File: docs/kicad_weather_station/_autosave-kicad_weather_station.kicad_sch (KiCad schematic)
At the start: 3 parts, among them U1 DHT11

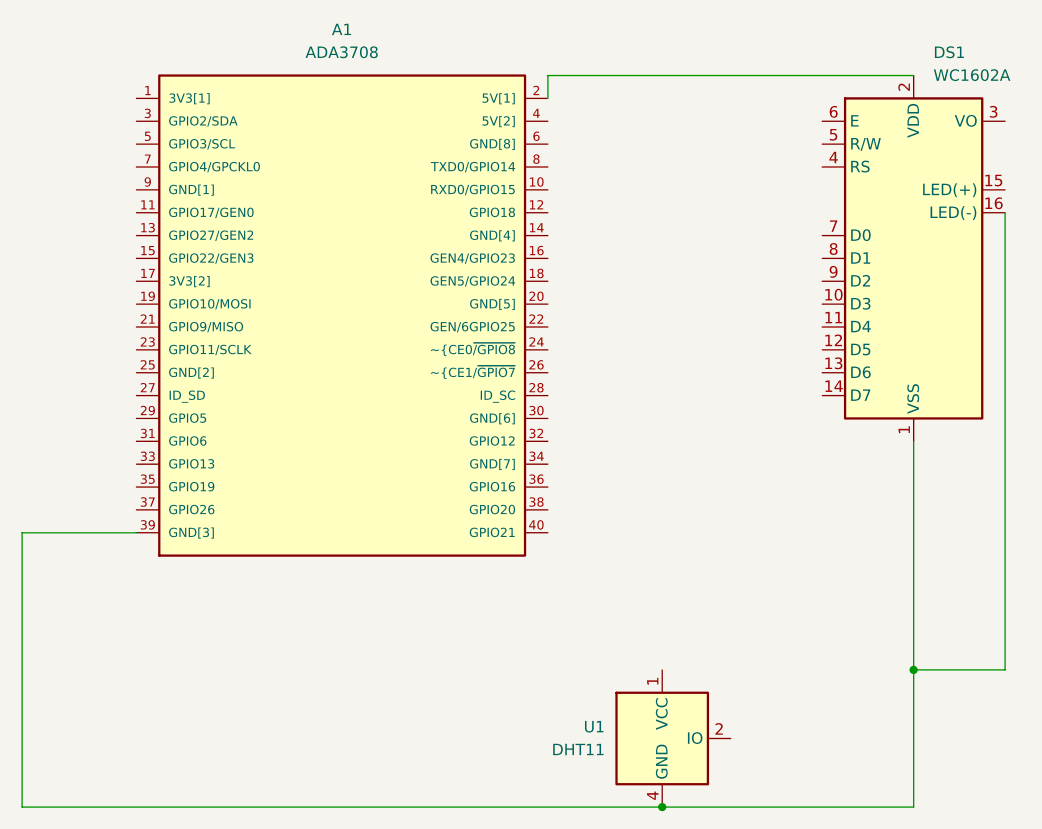
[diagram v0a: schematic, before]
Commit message: Updated README.md and updated parseString code
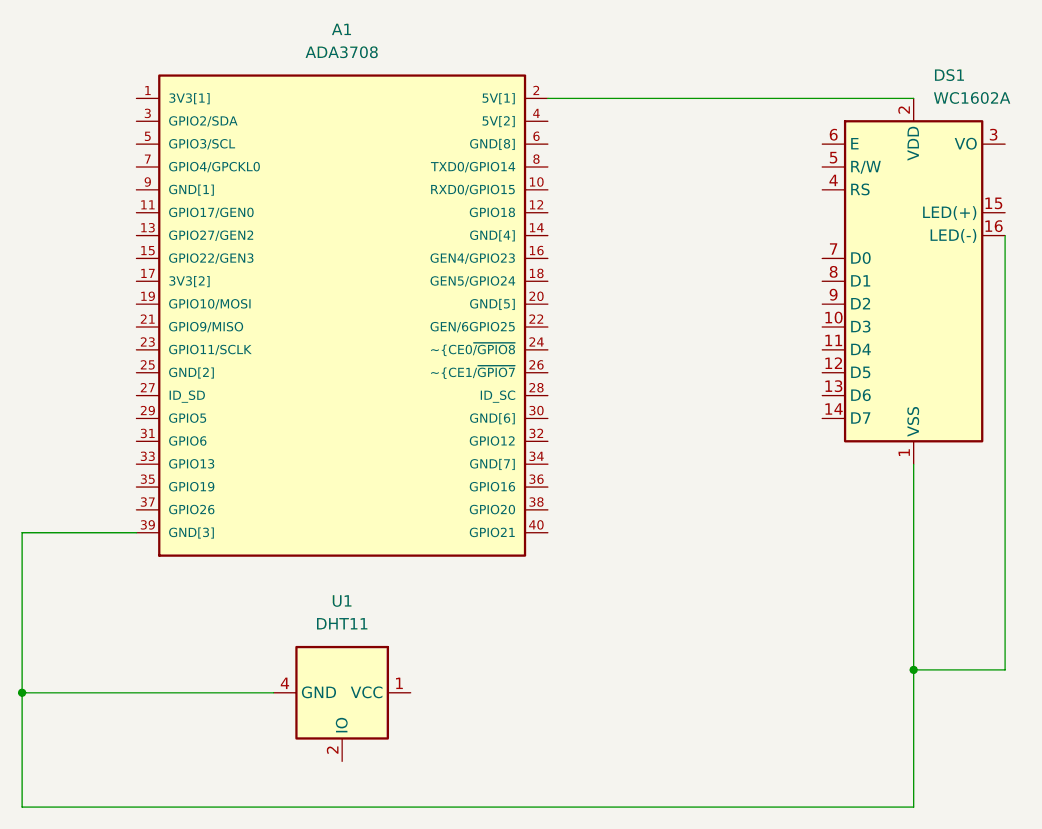
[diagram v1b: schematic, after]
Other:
- moved on the sheet: DS1, U1
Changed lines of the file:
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@@
 (kicad_sch (version 20230121) (generator eeschema)
   (paper "A4")
+  (junction (at 33.02 104.14) (diameter 0) (color 0 0 0 0)
+  )
   (junction (at 132.08 101.6) (diameter 0) (color 0 0 0 0)
   )
-  (junction (at 104.14 116.84) (diameter 0) (color 0 0 0 0)
-  )
-  (wire (pts (xy 104.14 116.84) (xy 33.02 116.84))
+  (wire (pts (xy 132.08 38.1) (xy 91.44 38.1))
     (stroke (width 0) (type default))
   )
-  (wire (pts (xy 132.08 35.56) (xy 91.44 35.56))
-    (stroke (width 0) (type default))
-  )
-  (wire (pts (xy 132.08 116.84) (xy 132.08 101.6))
-    (stroke (width 0) (type default))
-  )
-  (wire (pts (xy 33.02 116.84) (xy 33.02 86.36))
-    (stroke (width 0) (type default))
-  )
-  (wire (pts (xy 104.14 116.84) (xy 132.08 116.84))
+  (wire (pts (xy 33.02 86.36) (xy 33.02 104.14))
     (stroke (width 0) (type default))
   )
@@
     (stroke (width 0) (type default))
   )
-  (wire (pts (xy 142.24 50.8) (xy 142.24 101.6))
+  (wire (pts (xy 33.02 104.14) (xy 60.96 104.14))
+    (stroke (width 0) (type default))
+  )
+  (wire (pts (xy 142.24 53.34) (xy 142.24 101.6))
     (stroke (width 0) (type default))
   )
@@
     (stroke (width 0) (type default))
   )
-  (wire (pts (xy 91.44 35.56) (xy 91.44 38.1))
+  (wire (pts (xy 33.02 116.84) (xy 33.02 104.14))
     (stroke (width 0) (type default))
   )
-  (wire (pts (xy 132.08 76.2) (xy 132.08 101.6))
+  (wire (pts (xy 132.08 101.6) (xy 132.08 116.84))
     (stroke (width 0) (type default))
   )
-  (symbol (lib_id "Display_Character:WC1602A") (at 132.08 55.88 0) (unit 1)
+  (wire (pts (xy 132.08 78.74) (xy 132.08 101.6))
+    (stroke (width 0) (type default))
+  )
+  (wire (pts (xy 132.08 116.84) (xy 33.02 116.84))
+    (stroke (width 0) (type default))
+  )
+  (symbol (lib_id "Display_Character:WC1602A") (at 132.08 58.42 0) (unit 1)
     (in_bom yes) (on_board yes) (dnp no) (fields_autoplaced)
-    (property "Reference" "DS1" (at 134.2741 33.02 0)
+    (property "Reference" "DS1" (at 134.2741 35.56 0)
       (effects (font (size 1.27 1.27)) (justify left))
     )
-    (property "Value" "WC1602A" (at 134.2741 35.56 0)
+    (property "Value" "WC1602A" (at 134.2741 38.1 0)
       (effects (font (size 1.27 1.27)) (justify left))
     )
-    (property "Footprint" "TextBasedDisplay:WC1602A" (at 132.08 78.74 0)
+    (property "Footprint" "TextBasedDisplay:WC1602A" (at 132.08 81.28 0)
       (effects (font (size 1.27 1.27) italic) hide)
     )
-    (property "Datasheet" "http://www.wincomlcd.com/pdf/WC1602A-SFYLYHTC06.pdf" (at 149.86 55.88 0)
+    (property "Datasheet" "http://www.wincomlcd.com/pdf/WC1602A-SFYLYHTC06.pdf" (at 149.86 58.42 0)
       (effects (font (size 1.27 1.27)) hide)
     )
@@
     )
   )
-  (symbol (lib_id "Sensor:DHT11") (at 104.14 109.22 0) (unit 1)
+  (symbol (lib_id "Sensor:DHT11") (at 68.58 104.14 270) (unit 1)
     (in_bom yes) (on_board yes) (dnp no) (fields_autoplaced)
-    (property "Reference" "U1" (at 97.79 107.95 0)
-      (effects (font (size 1.27 1.27)) (justify right))
+    (property "Reference" "U1" (at 68.58 93.98 90)
+      (effects (font (size 1.27 1.27)))
     )
-    (property "Value" "DHT11" (at 97.79 110.49 0)
-      (effects (font (size 1.27 1.27)) (justify right))
+    (property "Value" "DHT11" (at 68.58 96.52 90)
+      (effects (font (size 1.27 1.27)))
     )
-    (property "Footprint" "Sensor:Aosong_DHT11_5.5x12.0_P2.54mm" (at 104.14 119.38 0)
+    (property "Footprint" "Sensor:Aosong_DHT11_5.5x12.0_P2.54mm" (at 58.42 104.14 0)
       (effects (font (size 1.27 1.27)) hide)
     )
-    (property "Datasheet" "http://akizukidenshi.com/download/ds/aosong/DHT11.pdf" (at 107.95 102.87 0)
+    (property "Datasheet" "http://akizukidenshi.com/download/ds/aosong/DHT11.pdf" (at 74.93 107.95 0)
       (effects (font (size 1.27 1.27)) hide)
     )
